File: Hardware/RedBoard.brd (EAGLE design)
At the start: 68.6 x 53.3 mm, 69 parts, among them IC3 LM1117, J1 microB, J2 ICSP, J3 POWER_JACKSUPER_BOMB_DIGITY, J4 SMD, Q1 1A/60V/500mΩ, Q2 2N7002PW, Q3 2N7002PW, U2 CH340G, U3 AP2112-3.3V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

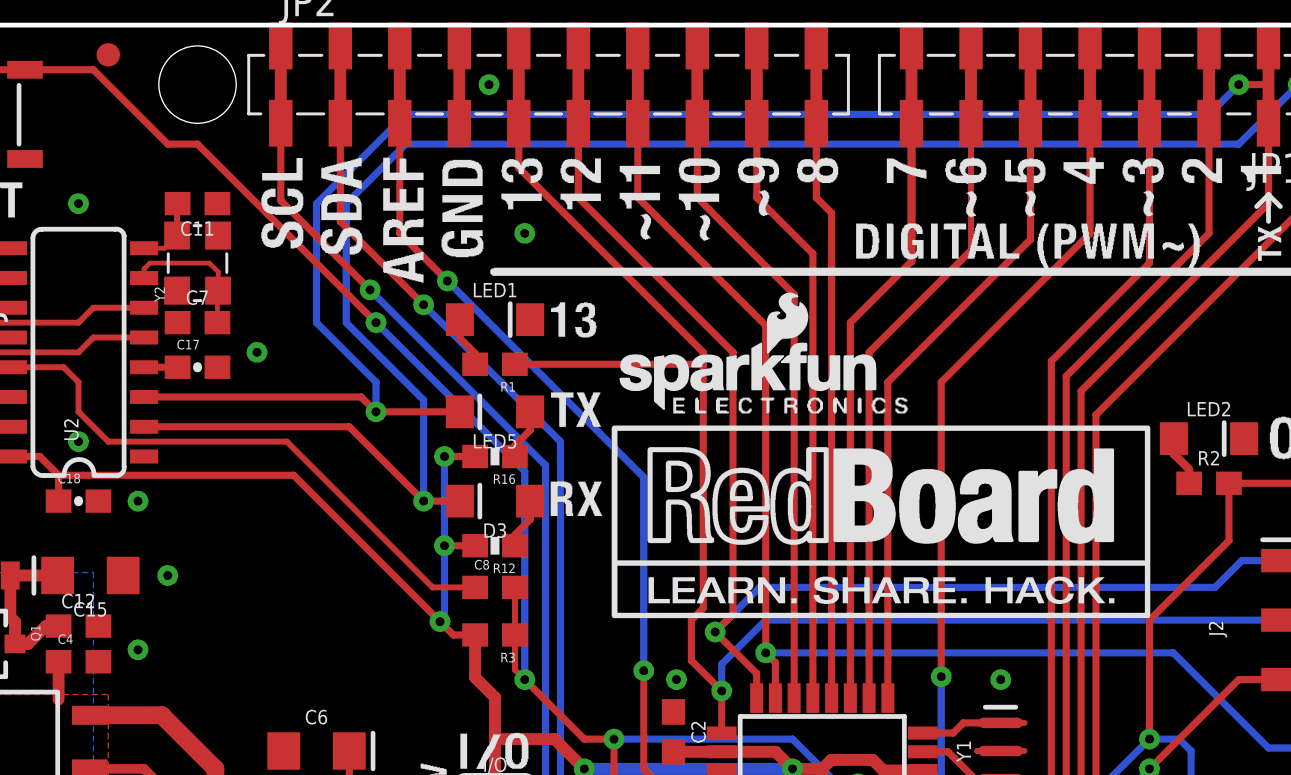
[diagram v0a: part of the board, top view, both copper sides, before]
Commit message: Silk Changes
"BlackBoard / Made In The USA" Silk Added
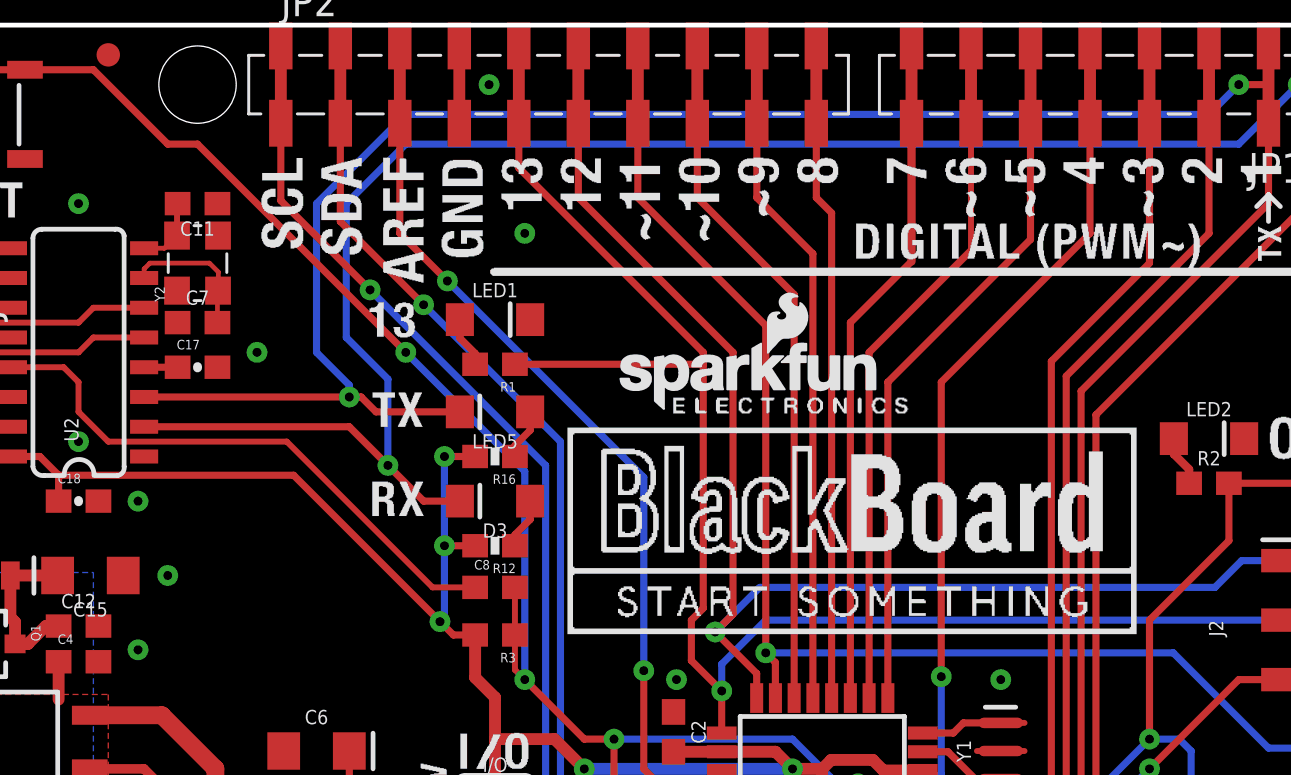
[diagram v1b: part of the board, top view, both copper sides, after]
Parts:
- added U$1, U$3: (no value), blackboardlogo:BLACKBOARDLOGO#PNG
- added U$4: (no value), madeinusa:MADEINUSA#PNG
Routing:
- net RX-I: track 122.4 -> 120.2 mm
- net TX-O: track 112.9 -> 111.8 mm
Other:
- board text removed: "ITALY"
- board text removed: "MADE IN"
